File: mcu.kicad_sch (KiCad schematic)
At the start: 42 parts, among them J2 USB-C, J3 UART0, J4 I2C / Qwiic, J5 SPI, J6 WS2812, J7 Spare IO, J8 Rail break-out, Q4 AO3401A, Q5 MMBT3906, SW1 RESET, SW2 BOOT, U5 ESP32-S3-WROOM-1-N16R8, U6 TLV431A, U7 USBLC6-2SC6, U8 USBLC6-2SC6, U9 74AHCT1G125

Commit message: Re-scope the fork as a carrier board: no power section, differential analog, K-line
The shield idea does not survive measurement. Component courtyard on the
parent is 3052 mm2 over an 84 x 100 board -- 36% packing, not the 50% I had
been estimating -- and a DevKitC-1 is 63 x 25.5 = 1607 mm2. The parts alone
were 1.4x the whole dev board. So this is a carrier the dev board plugs into,
not a shield that fits on top of one.

Power section deleted entirely. It was 1746 mm2, 57% of the board, for two
rails the DevKitC-1 already makes from its USB-C. Gone: both LM5164 bucks and
everything around them, the LM74700 ideal diode, the reverse-battery FET, the
three electrolytic cans, the 12 V input, and the sensor-rail load switch.
Both rails are now inputs, taken up through the sockets -- which reverses the
earlier "feed 5 V only" rule, because there is no longer a second regulator
to parallel against.

Hold-up is a supercapacitor, not electrolytics. The first sizing was wrong:
energy goes as V-squared and the usable window at 5 V is 4.2 -> 3.6 V, so
2000 uF buys 12.5 ms, not the ~50 ms claimed. 0.5 F over the same window is
2.5 s, in less area than one of the 100 V cans it replaces. Low-ESR
cylindrical cells specifically -- coin EDLCs are 30-200 ohm and cannot source
120 mA at all.

Analog runs differentially. The board is grounded twice now, through the
sensor loom and through USB by way of a charger elsewhere in the car, and a
few hundred mV of chassis drop is 6% of a 0-5 V channel -- which makes the
0.1% dividers pointless. The correction has to be at the divider, not the
ADC, so the sensor ground comes back as a Kelvin wire through a matched
attenuator. Two ADS1115s, because one MUX only offers three channels against
a shared negative.

K-line added, discrete rather than an L9637D: that part's TXD threshold is
0.7*VCC = 3.5 V and a 3.3 V GPIO cannot meet it. Low-side 2N7002, clamped
22k/10k receiver, optional ISO 9141 tester pull-up on a jumper.

Pin map regrouped by boa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
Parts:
- removed C26: 1uF, Capacitor_SMD:C_0805_2012Metric, symbol Device:C
- removed C27, C30: 10uF, Capacitor_SMD:C_1206_3216Metric, symbol Device:C
- removed C28, C29, C31, C32: 100nF, Capacitor_SMD:C_0805_2012Metric, symbol Device:C
- removed D5: 40V 1A, Diode_SMD:D_SOD-123, symbol Device:D_Schottky
- removed J7: Spare IO, Connector_PinHeader_2.54mm:PinHeader_1x06_P2.54mm_Vertical, symbol Connector_Generic:Conn_01x06
- removed J8: Rail break-out, Connector_PinHeader_2.54mm:PinHeader_1x04_P2.54mm_Vertical, symbol Connector_Generic:Conn_01x04
- removed PF3: 0.5A hold, Resistor_SMD:R_1206_3216Metric, symbol Device:Polyfuse
- removed Q4: AO3401A, Package_TO_SOT_SMD:SOT-23, symbol Transistor_FET:Q_PMOS_GSD
- removed Q5: MMBT3906, Package_TO_SOT_SMD:SOT-23, symbol Transistor_BJT:Q_PNP_BEC
- removed R23, R24, R28, R33, R36, R37, R38: 10k, Resistor_SMD:R_0805_2012Metric, symbol Device:R
- removed R25, R26: 5.1k, Resistor_SMD:R_0805_2012Metric, symbol Device:R
- removed R27, R29: 100k, Resistor_SMD:R_0805_2012Metric, symbol Device:R
- removed R30: 27.4k, Resistor_SMD:R_0805_2012Metric, symbol Device:R
- removed R31, R32: 4.7k, Resistor_SMD:R_0805_2012Metric, symbol Device:R
- removed R34: 33, Resistor_SMD:R_0805_2012Metric, symbol Device:R
- removed R35: 100, Resistor_SMD:R_0805_2012Metric, symbol Device:R
- removed SW1: RESET, Button_Switch_SMD:SW_SPST_TL3342, symbol Switch:SW_Push
- removed SW2: BOOT, Button_Switch_SMD:SW_SPST_TL3342, symbol Switch:SW_Push
- removed U5: ESP32-S3-WROOM-1-N16R8, RF_Module:ESP32-S3-WROOM-1, symbol RF_Module:ESP32-S3-WROOM-1
- removed U6: TLV431A, Package_TO_SOT_SMD:SOT-23, symbol Reference_Voltage:TL431DBZ
- removed U7, U8: USBLC6-2SC6, Package_TO_SOT_SMD:SOT-23-6, symbol Power_Protection:USBLC6-2SC6
- removed U9: 74AHCT1G125, Package_TO_SOT_SMD:SOT-23-5, symbol 74xGxx:74AHCT1G125
- added C10: 10uF, Capacitor_SMD:C_1206_3216Metric, symbol Device:C
- added C11, C12: 100nF, Capacitor_SMD:C_0805_2012Metric, symbol Device:C
- added R10, R9: 4.7k, Resistor_SMD:R_0805_2012Metric, symbol Device:R
- added R11: 33, Resistor_SMD:R_0805_2012Metric, symbol Device:R
- added R12: 100, Resistor_SMD:R_0805_2012Metric, symbol Device:R
- added U2: 74AHCT1G125, Package_TO_SOT_SMD:SOT-23-5, symbol 74xGxx:74AHCT1G125
- J2: value USB-C -> DevKit J1; footprint Connector_USB:USB_C_Receptacle_HRO_TYPE-C-31-M-12 -> Connector_PinSocket_2.54mm:PinSocket_1x22_P2.54mm_Vertical; symbol Connector:USB_C_Receptacle_USB2.0_16P -> Connector_Generic:Conn_01x22; MPN HRO TYPE-C-31-M-12 -> ESP32-S3-DevKitC-1 J1; Note Programming / CDC console only -- not a power path in the c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 -> Mirrors DevKitC-1 J1. Pins 1-2 (3V3) and 21 (5V) are both I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
- J3: value UART0 -> DevKit J3; footprint Connector_PinHeader_2.54mm:PinHeader_1x04_P2.54mm_Vertical -> Connector_PinSocket_2.54mm:PinSocket_1x22_P2.54mm_Vertical; symbol Connector_Generic:Conn_01x04 -> Connector_Generic:Conn_01x22; MPN (none) -> ESP32-S3-DevKitC-1 J3; Note (none) -> Mirrors DevKitC-1 J3. K-line on 6/7, I2C on 9/17, WS2812 on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
- J4: Note (none) -> External I2C sensors. Kept because the dev board has no Qwi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
- J5: value SPI -> WS2812; footprint Connector_PinHeader_2.54mm:PinHeader_1x06_P2.54mm_Vertical -> Connector_PinHeader_2.54mm:PinHeader_1x03_P2.54mm_Vertical; symbol Connector_Generic:Conn_01x06 -> Connector_Generic:Conn_01x03; Note IO40 SCK / IO41 MISO / IO42 MOSI / IO47 CS -- GPIO-matrix S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 -> Shift-light header: +5V / 5V-logic DIN / GND
- J6: value WS2812 -> Rail break-out; footprint Connector_PinHeader_2.54mm:PinHeader_1x03_P2.54mm_Vertical -> Connector_PinHeader_2.54mm:PinHeader_1x04_P2.54mm_Vertical; symbol Connector_Generic:Conn_01x03 -> Connector_Generic:Conn_01x04; Note Shift-light header: +5V / 5V-logic DIN / GND -> (none)
- PF2: Note (none) -> Fused tap for the shift-light strip (8x WS2812 ~0.5 A worst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
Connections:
- net SPI_SCK is gone; now on net GND: J5.3 (Pin_3)
- net VBUS_R is gone; now on net LED_5V: PF2.2
- net +3V3: now also J2.1 (Pin_1), J2.2 (Pin_2), J6.2 (Pin_2), C10.1, C11.1, R10.1, R9.1; no longer J3.1 (Pin_1), J5.1 (Pin_1)
- net +5V: now also J2.21 (Pin_21), J6.1 (Pin_1), PF2.1, C12.1, U2.5 (VCC)
- net AIN1: now also J2.4 (Pin_4)
- net AIN2: now also J2.5 (Pin_5)
- net AIN3: now also J2.6 (Pin_6)
- net AIN4: now also J2.7 (Pin_7)
- net CAN_RX: now also J2.11 (Pin_11)
- net CAN_S: now also J2.9 (Pin_9)
- net CAN_TX: now also J2.10 (Pin_10)
- net GND: now also J2.22 (Pin_22), J3.1 (Pin_1), J3.21 (Pin_21), J3.22 (Pin_22), J6.4 (Pin_4), C10.2, C11.2, C12.2, U2.1, U2.3 (GND); no longer J2.A1 (GND), J2.A12 (GND), J2.B1 (GND), J2.B12 (GND), J2.S1 (SHIELD), J3.4 (Pin_4), J5.2 (Pin_2)
- net I2C_SCL: now also J3.9 (Pin_9), R10.2
- net I2C_SDA: now also J3.17 (Pin_17), R9.2
- net LED_5V: now also J5.1 (Pin_1); no longer J6.1 (Pin_1)
- net LED_DIN: now also R12.1, U2.4
- net LED_DIN_A: now also R11.2, U2.2
- net LED_DIN_J: now also J5.2 (Pin_2), R12.2; no longer J6.2 (Pin_2)
- net LED_DIN_MCU: now also J3.16 (Pin_16), R11.1
- net PWR_FAIL: now also J2.8 (Pin_8)
- net SD_CD: now also J3.18 (Pin_18)
- net SD_CLK: now also J2.20 (Pin_20)
- net SD_CMD: now also J2.19 (Pin_19)
- net SD_D0: now also J2.18 (Pin_18)
- net SD_D1: now also J2.17 (Pin_17)
- net SD_D2: now also J2.16 (Pin_16)
- net SD_D3: now also J2.15 (Pin_15)
- net SD_PWR_EN: now also J3.8 (Pin_8)
- net VBAT_SNS: now also J2.12 (Pin_12)
- removed net SPI_CS: J5.6 (Pin_6)
- removed net SPI_MISO: J5.4 (Pin_4)
- removed net SPI_MOSI: J5.5 (Pin_5)
- net UART_RX: no longer names the net of J3.3 (Pin_3)
- net UART_TX: no longer names the net of J3.2 (Pin_2)
- removed net USB_CC1: J2.A5 (CC1)
- removed net USB_CC2: J2.B5 (CC2)
- removed net USB_DM_CON: J2.A7 (D-), J2.B7 (D-)
- removed net USB_DP_CON: J2.A6 (D+), J2.B6 (D+)
- removed net VBUS_IN: J2.A4 (VBUS), J2.A9 (VBUS), J2.B4 (VBUS), J2.B9 (VBUS), PF2.1
- new net K_RX: J3.6 (Pin_6)
- new net K_TX: J3.7 (Pin_7)
- no-connect marks 7 -> 15
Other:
- moved on the sheet: J4, PF2

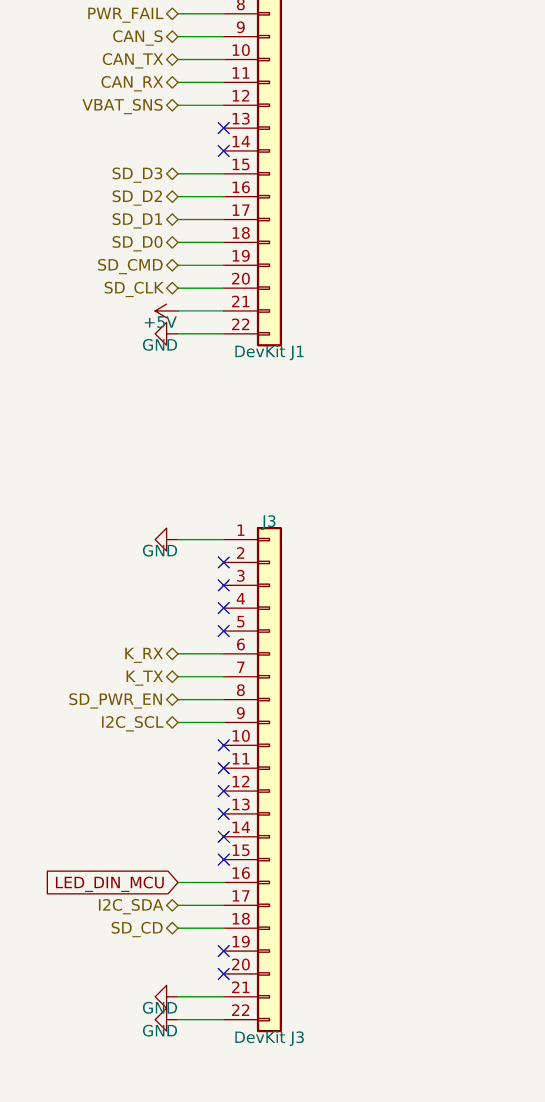
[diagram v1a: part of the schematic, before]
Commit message: Second CAN bus, single analog range, and three placement bugs the render caught
TWO CAN BUSES AT ONCE NEEDS A SECOND CONTROLLER. The ESP32-S3 has exactly
one TWAI peripheral. Two transceivers on it would give a bus you can pick at
runtime through the GPIO matrix, never two live at once, and the point of a
second bus is watching the powertrain and the body bus together. So the
second channel is an MCP2518FD on SPI (SOIC-14, KiCad ships the pin-compatible
MCP2517FD symbol) with its own 40 MHz crystal, its own TJA1051 -- same part
as CAN 1, so two positions on one BOM line -- choke, split termination and
clamps.

That cost five pins against two spare. The three came from dropping the
microSD to 1-bit SDMMC, which measurement says is free: the busiest case this
logger will see is ~128 kB/s against 1-bit's ~1500 kB/s, and bus width does
not touch the card's internal write stall, which is the only thing the
hold-up budget is actually sized around. The card keeps its D1/D2/D3
pull-ups because a card samples DAT3 at power-up and drops into SPI mode if
it finds it low -- they simply stop at the socket now.

Jumpers on the aux harness pins pick K-line or the second CAN pair, because
those two genuinely cannot share a wire: K-line idles at battery voltage and
a CAN transceiver biases its bus to 2.5 V. The clamps sit ahead of the
jumpers so the protection is the same either way, which also let the K-line
drop its own TVS. Default is K-line, which is what an R53 wants.

ANALOG DOWN TO ONE RANGE. The bypass and range-select jumpers are gone --
twelve jumpers and four resistors -- and every channel is a fixed 2.21/13.21
divider spanning 0-16 V, so a 5 V and a 12 V sensor both fit without
touching anything. Resolution was never the reason for a narrower range: a
5 V sensor lands at 0.836 V, which on a 16-bit ADS1115 is 6688 counts.

The real reason is the differential ground. A channel switched to 0-16 V
while the shared return attenuator stayed at the 0-5 V ratio subtracts
0.5769*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
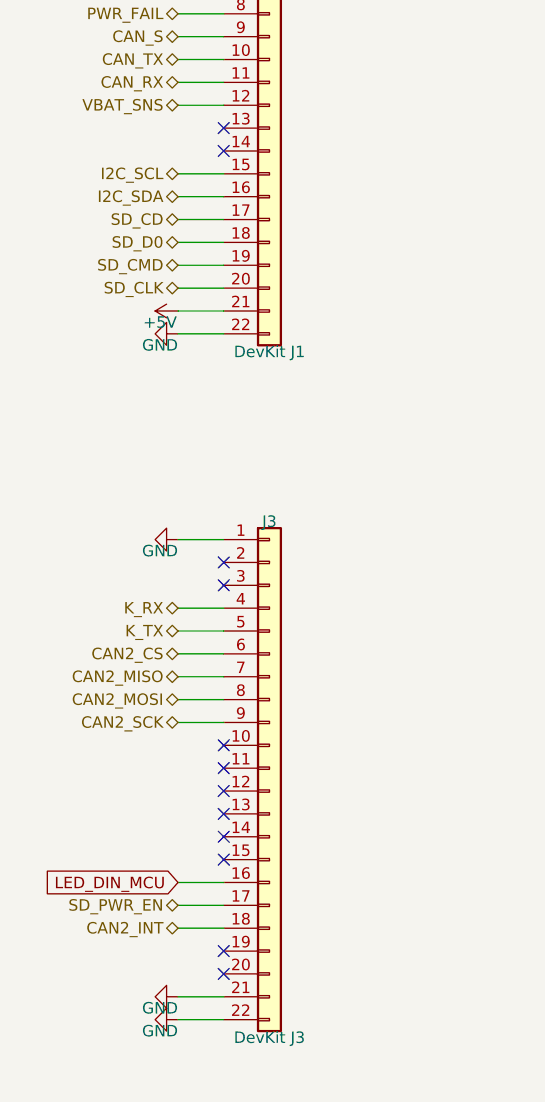
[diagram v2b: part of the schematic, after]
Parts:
- J3: Note Mirrors DevKitC-1 J3. K-line on 6/7, I2C on 9/17, WS2812 on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 -> Mirrors DevKitC-1 J3. K-line on 4/5, the second CAN's SPI o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
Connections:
- net SD_D1 is gone; now on net SD_CD: J2.17 (Pin_17)
- net SD_D2 is gone; now on net I2C_SDA: J2.16 (Pin_16)
- net SD_D3 is gone; now on net I2C_SCL: J2.15 (Pin_15)
- net I2C_SCL: no longer J3.9 (Pin_9)
- net I2C_SDA: no longer J3.17 (Pin_17)
- net K_RX: now also J3.4 (Pin_4); no longer J3.6 (Pin_6)
- net K_TX: now also J3.5 (Pin_5); no longer J3.7 (Pin_7)
- net SD_CD: no longer J3.18 (Pin_18)
- net SD_PWR_EN: now also J3.17 (Pin_17); no longer J3.8 (Pin_8)
- new net CAN2_CS: J3.6 (Pin_6)
- new net CAN2_INT: J3.18 (Pin_18)
- new net CAN2_MISO: J3.7 (Pin_7)
- new net CAN2_MOSI: J3.8 (Pin_8)
- new net CAN2_SCK: J3.9 (Pin_9)
- no-connect marks 15 -> 13
